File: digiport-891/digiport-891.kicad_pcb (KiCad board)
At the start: 2 copper layers, 40 x 22.8 mm, 45 parts, among them J1 USB_C_Receptacle_USB2.0_16P, J2 PJ-320A, J3 PJ-320A, Q1 MMBT5551L, Q2 MMBT5551L, U1 USB2412-DZK-TR, U2 CM108B, Y1 24MHz

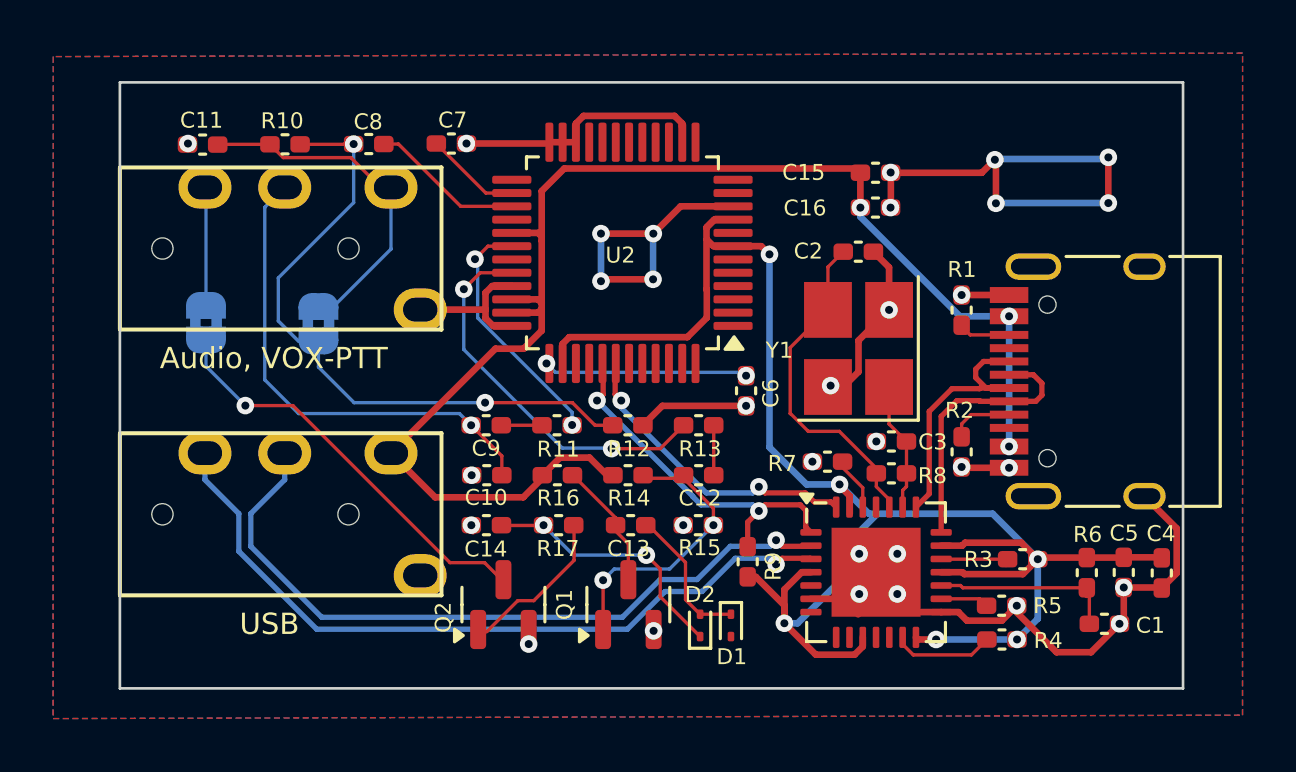
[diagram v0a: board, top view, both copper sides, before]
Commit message: v2：优化PCB布局，将RIG_AFIN和RIG_AFOUT移动到音频接插件附近，减少过孔数量， 避免焊盘上的过孔。
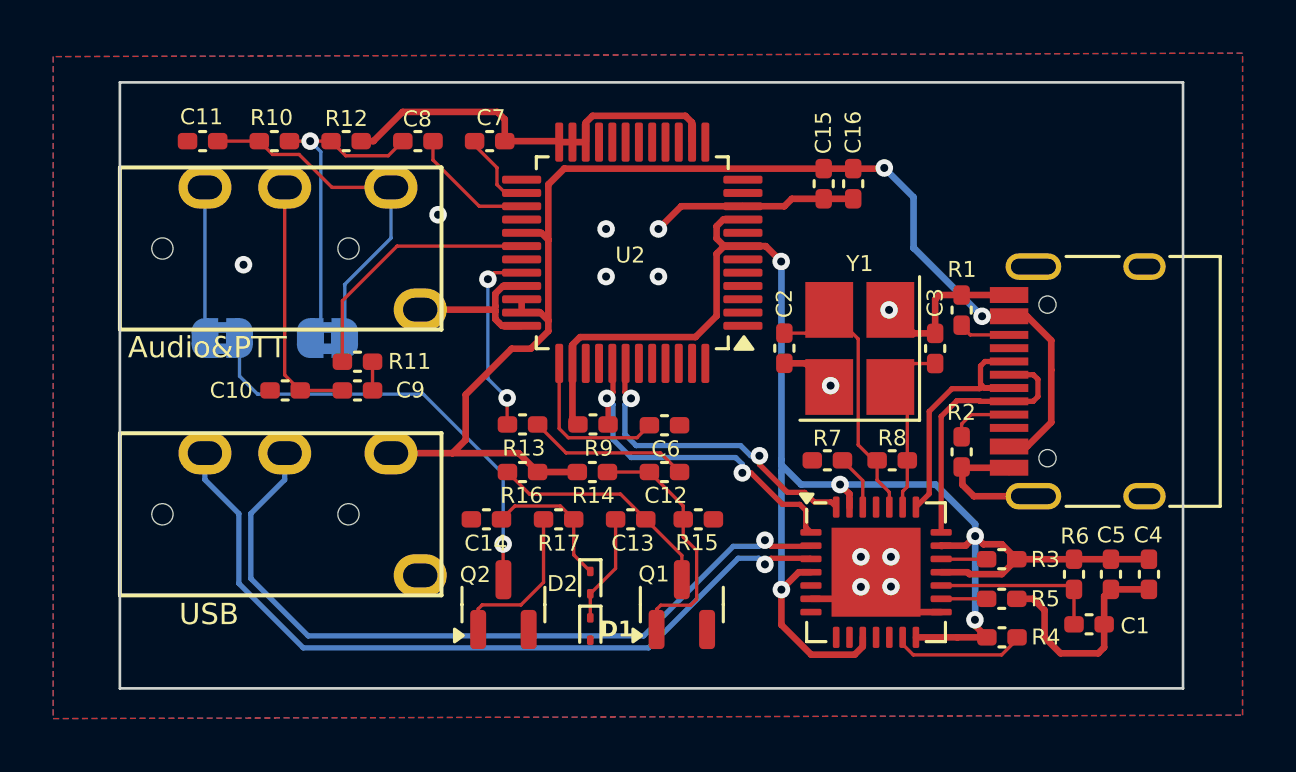
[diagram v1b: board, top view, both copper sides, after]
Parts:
- moved R12 15.1 mm to (117.0, 102.6)
- moved C10 8.23 mm to (114.7, 111.9)
- moved R11 7.88 mm to (117.4, 110.9), turned to 0 degrees
- moved R9 7.78 mm to (126.3, 113.2), turned to 0 degrees
- moved R13 6.63 mm to (123.6, 113.2)
- moved D1 5.29 mm to (126.2, 120.9)
- moved C9 5.02 mm to (117.4, 111.9)
- moved C2 4.58 mm to (133.5, 110.4), turned to -90 degrees
- moved D2 4.43 mm to (126.2, 119.2), turned to -90 degrees
- moved C3 3.87 mm to (139.2, 110.4), turned to 90 degrees
- moved C6 3.33 mm to (129.0, 113.2), turned to 0 degrees
- moved Q1 2.01 mm to (129.6, 120.0)
- moved C15 1.99 mm to (135.0, 104.2), turned to -90 degrees
- moved C8 1.85 mm to (119.7, 102.6)
- moved C7 1.44 mm to (122.4, 102.6)
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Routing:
- net GND: track 86.9 -> 65.7 mm, vias 32 -> 12
- net Net-(JP1-A): track 24.6 -> 12.7 mm, vias 2 -> 1
- net /RIG_AFIN: track 18.3 -> 9.91 mm, vias 1 -> 0
- net ROUT: track 14.5 -> 7.14 mm
- net +3V3: track 69.2 -> 63.1 mm, vias 6 -> 5
- net Net-(U1-XTAL_OUT): track 4.85 -> 9.26 mm
- net Net-(D2-K): track 9.54 -> 5.35 mm, vias 2 -> 0
- net Net-(C12-Pad1): track 2.00 -> 6.08 mm
- net Net-(Q1-C): track 4.98 -> 8.77 mm
- net Net-(U1-XTAL_IN): track 12.7 -> 10.5 mm
- net VOX-PTT: track 4.57 -> 6.35 mm
- net Net-(U2-AREG36): track 7.82 -> 6.19 mm, vias 2 -> 0
- net Net-(U2-MICIN): track 6.30 -> 4.99 mm
- net Net-(JP2-B): track 15.5 -> 16.9 mm
- net /USBDN2_D+: track 28.3 -> 29.6 mm
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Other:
- board text added: "Audio&PTT"
- board text removed: "Audio, VOX-PTT"

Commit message: 优化PCB布线
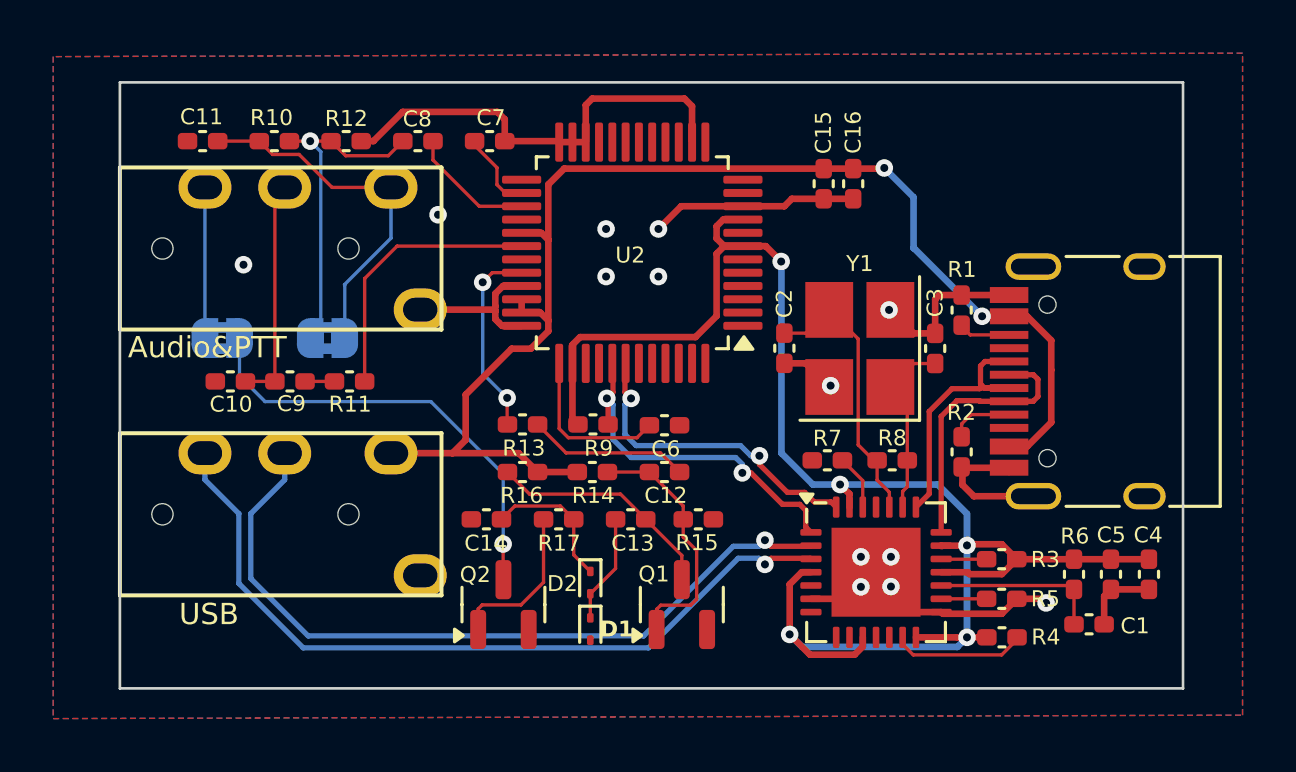
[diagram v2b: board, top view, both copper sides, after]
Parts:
- moved C9 2.56 mm to (114.9, 111.6)
- moved C10 2.09 mm to (112.7, 111.6)
- moved R11 0.80 mm to (117.1, 111.6), turned to 180 degrees
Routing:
- net +3V3: track 63.1 -> 64.3 mm
- net /RIG_AFIN: track 9.91 -> 9.00 mm
- net GND: track 65.7 -> 65.6 mm, vias 12 -> 13

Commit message: cable pinout file added
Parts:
- turned Q1 to 0 degrees
- turned Q2 to 0 degrees
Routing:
- net Net-(Q1-C): track 8.77 -> 12.4 mm
- net Net-(Q1-B): track 9.55 -> 6.55 mm
- net Net-(Q2-B): track 6.02 -> 3.85 mm
- net Net-(JP2-B): track 16.9 -> 18.2 mm
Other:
- board text added: "DigiPort-891 v2 参考DigiRig DR-891,移除GPIO控制PTT Redesigned by BD5HLI, 2025.2"
- board text removed: "参考DigiRig DR-891 移除GPIO控制PTT Redesign by BD5HLI 2024.12"

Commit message: C12 value corrected.
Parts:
- C14: value 1nF -> 1uF
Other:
- board text added: "JLCJLCJLCJLC"
